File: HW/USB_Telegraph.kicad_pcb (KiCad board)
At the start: 2 copper layers, 50 x 25 mm, 34 parts, among them J1 USB_C_Receptacle_USB2.0, J2 Conn_02x05_Odd_Even, J3 Screw_Terminal_01x01, J4 Screw_Terminal_01x01, J5 Conn_01x03, Q1 NP2302FVR, U1 STM32F103C8Tx, U2 XC6206PxxxMR, U4 USBLC6-2SC6, Y1 8MHz

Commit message: Initial routing
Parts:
- J1: footprint Connector_USB:USB_C_Receptacle_G-Switch_GT-USB-7010ASV -> Connectors:USB_C_Receptacle_G-Switch_GT-USB-7010ASV
- moved J5 178.4 mm to (148.4, 115.0), turned to 180 degrees
- moved R12 11.1 mm to (128.5, 102.9)
- moved R13 11.0 mm to (128.4, 104.0)
- moved C5 2.29 mm to (122.9, 110.2), turned to -135 degrees
- moved C6 2.21 mm to (134.8, 114.7), turned to 45 degrees
- moved J3 2.05 mm to (141.9, 112.5)
- moved C4 2.02 mm to (127.0, 118.6), turned to -45 degrees
- moved U4 1.94 mm to (112.4, 119.6)
- moved RV1 1.72 mm to (140.9, 121.3)
- moved C7 1.49 mm to (108.1, 109.8)
- moved R6 1.11 mm to (108.1, 113.9), turned to 90 degrees
- moved R1 0.86 mm to (126.3, 105.0)
- moved J4 0.48 mm to (114.5, 112.5)
- moved C8 0.20 mm to (122.7, 114.3)
- moved R5 0.11 mm to (108.1, 111.8)
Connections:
- net /USB_DM renamed /USB_DN
- net /USB_DM_ST renamed /USB_ST_DN
- net /USB_DP_ST renamed /USB_ST_DP
- J1 pad S1: unconnected-(J1-SHIELD-PadS1) -> GND
- J5 pad 1: unconnected-(J5-Pin_1-Pad1) -> /SWDIO
- J5 pad 2: unconnected-(J5-Pin_2-Pad2) -> /SWDCLK
- J5 pad 3: unconnected-(J5-Pin_3-Pad3) -> GND
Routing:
- net +3V3: track 0.00 -> 50.3 mm
- net Net-(D1-K): track 0.00 -> 46.7 mm, vias 0 -> 3
- net /SWDIO: track 0.00 -> 45.0 mm, vias 0 -> 7
- net /SWDCLK: track 0.00 -> 43.2 mm, vias 0 -> 5
- net +5V: track 0.00 -> 35.4 mm
- net GND: track 0.00 -> 33.5 mm, vias 0 -> 31
- net Net-(D1-A): track 0.00 -> 31.0 mm
- net /SWO: track 0.00 -> 20.0 mm, vias 0 -> 2
- net /USB_DP: track 0.00 -> 19.9 mm
- net /USB_DN: track 2.86 -> 19.3 mm, vias 0 -> 2
- net /USB_ST_DP: track 0.00 -> 14.0 mm
- net /USB_ST_DN: track 0.00 -> 13.4 mm
- net /RST: track 0.00 -> 12.3 mm, vias 0 -> 4
- net /SENSE2: track 0.00 -> 12.0 mm, vias 0 -> 4
- net /SENSE1: track 0.00 -> 7.93 mm
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- added copper zone on B.Cu, net GND
- added copper zone on F.Cu, net GND

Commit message: Routing done, part assignement done
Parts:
- RV1: footprint Potentiometer_SMD:Potentiometer_Bourns_TC33X_Vertical -> Potentiometer_SMD:Potentiometer_Bourns_3314J_Vertical
- moved R10 1.50 mm to (112.5, 105.6)
- moved RV1 0.49 mm to (141.3, 121.1), turned to 90 degrees
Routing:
- net Net-(D1-K): track 46.7 -> 45.2 mm
- net +5V: track 35.4 -> 33.9 mm
- net Net-(D1-A): track 31.0 -> 32.1 mm
- net GND: track 33.5 -> 33.9 mm, vias 31 -> 164

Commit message: minor pcb changes
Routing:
- net +3V3: track 50.8 -> 52.7 mm
- net GND: vias 164 -> 194

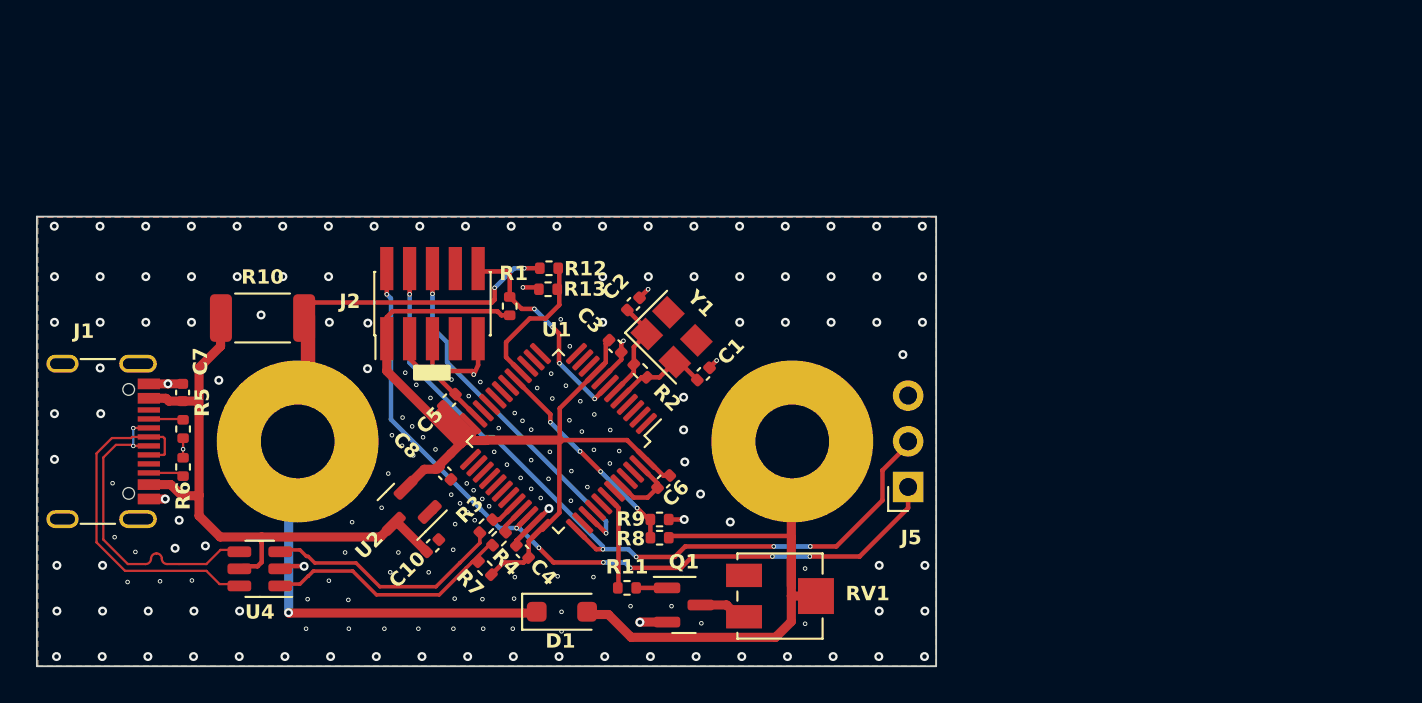
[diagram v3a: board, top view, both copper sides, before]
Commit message: changed via size
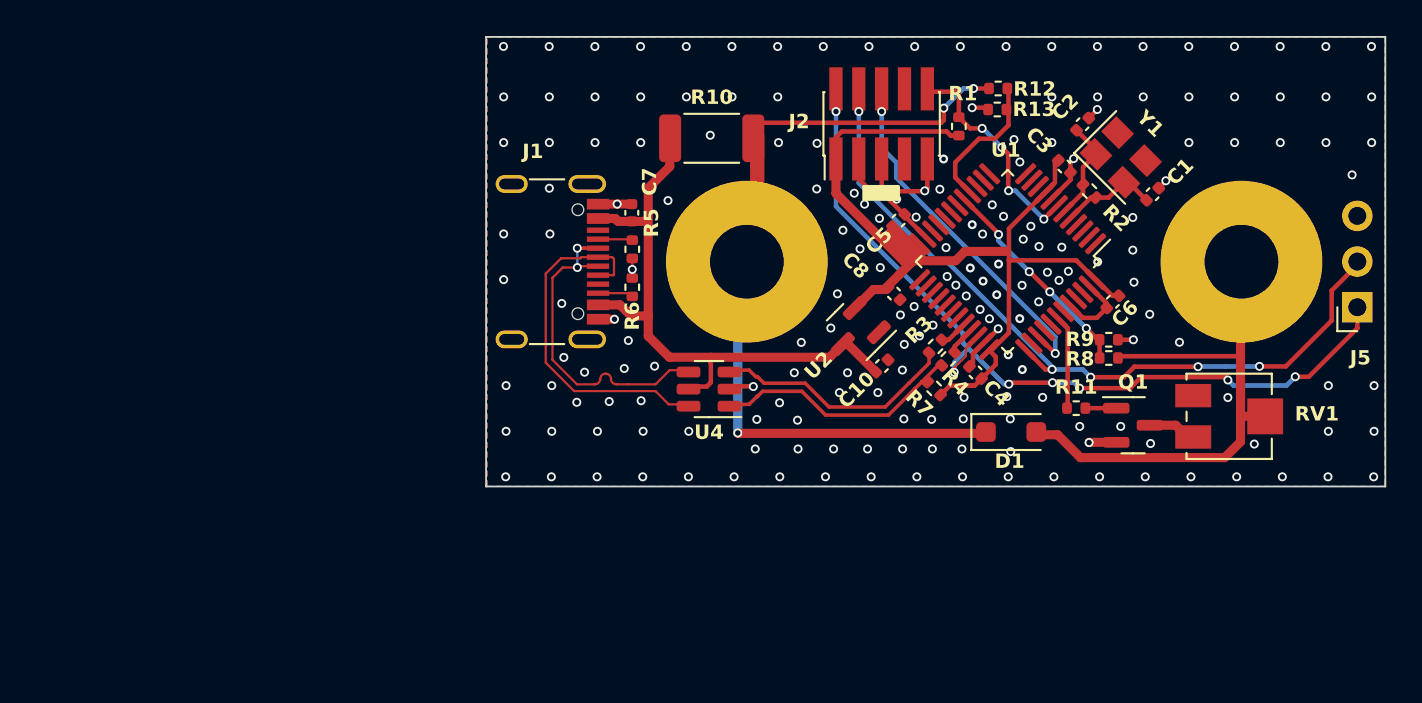
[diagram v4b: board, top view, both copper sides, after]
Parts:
- moved C4 27.1 mm to (152.2, 108.7)
- moved Q1 26.9 mm to (160.9, 111.6)
- moved R11 26.9 mm to (157.8, 110.6)
- moved R12 26.9 mm to (153.4, 92.9)
- moved R2 26.9 mm to (158.5, 98.6)
- moved RV1 26.9 mm to (166.3, 111.1)
- moved J3 26.9 mm to (166.9, 102.5)
- moved J5 26.9 mm to (173.4, 105.0)
- moved R3 26.9 mm to (150.0, 107.2)
- moved Y1 26.9 mm to (160.3, 96.7)
- moved C10 26.9 mm to (147.0, 108.3)
- moved C7 26.9 mm to (133.1, 99.8)
- moved C8 26.9 mm to (147.7, 104.3)
- moved R1 26.9 mm to (151.3, 95.0)
- moved R5 26.9 mm to (133.1, 101.8)
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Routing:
- net +3V3: track 52.7 -> 56.2 mm
- net /SWDIO: track 45.0 -> 47.2 mm
- net GND: track 33.9 -> 32.1 mm, vias 194 -> 187
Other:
- board text added: "0.1270 mm / 0.1270 mm"
- board text added: "0.1500 mm"
- board text added: "1.6000 mm"
- board text added: "2"
- board text added: "50.0000 mm x 25.0000 mm"
- board text added: "BOARD CHARACTERISTICS"
- board text added: "Board Thickness:"
- board text added: "Board overall dimensions:"
- board text added: "Castellated pads:"
- board text added: "Copper Finish:"
- board text added: "Copper Layer Count:"
- board text added: "Edge card connectors:"
- board text added: "HAL lead-free"
- board text added: "Impedance Control:"
- board text added: "Min hole diameter:"
- board text added: "Min track/spacing:"
- board text added: "No"
- board text added: "Plated Board Edge:"
